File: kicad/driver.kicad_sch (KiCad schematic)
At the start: 72 parts, among them Q1 IRFZ44N, Q2 IRFZ44N, Q3 IRFZ44N, Q4 IRFZ44N, Q5 IRFZ44N, Q6 IRFZ44N, U1 IR2104, U2 IR2104, U3 IR2104, U4 INA180A2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

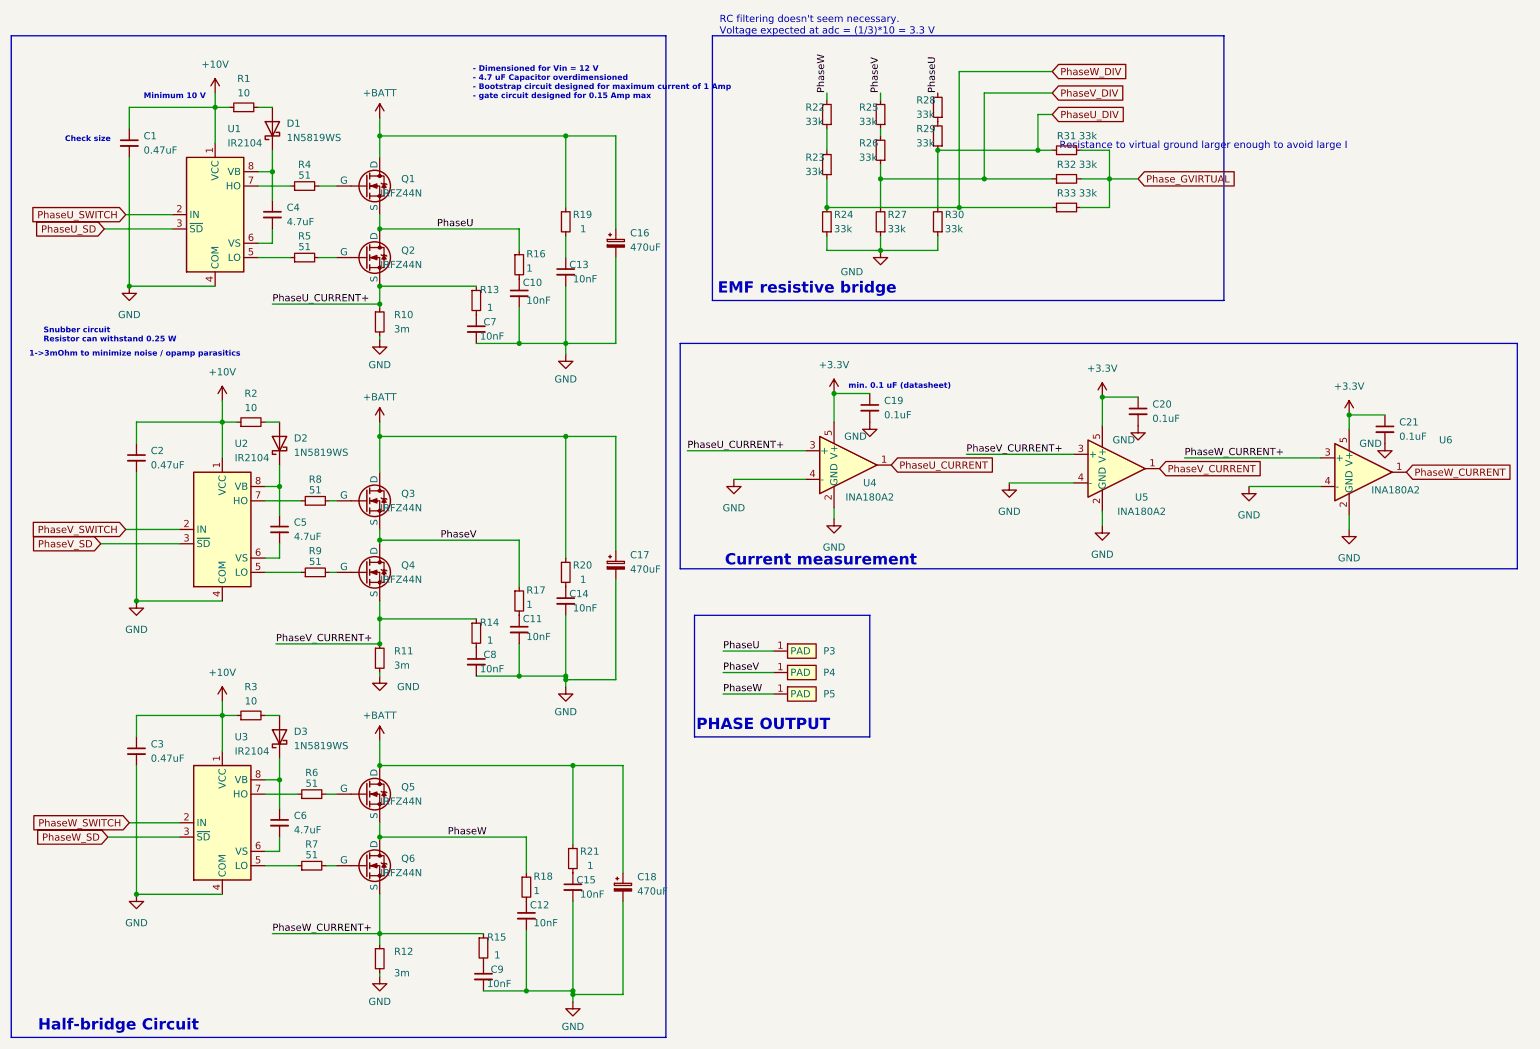
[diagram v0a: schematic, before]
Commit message: [bldc] Fixed footprint issues, added jlcpcb man. rules, stackup decisions, added nets..
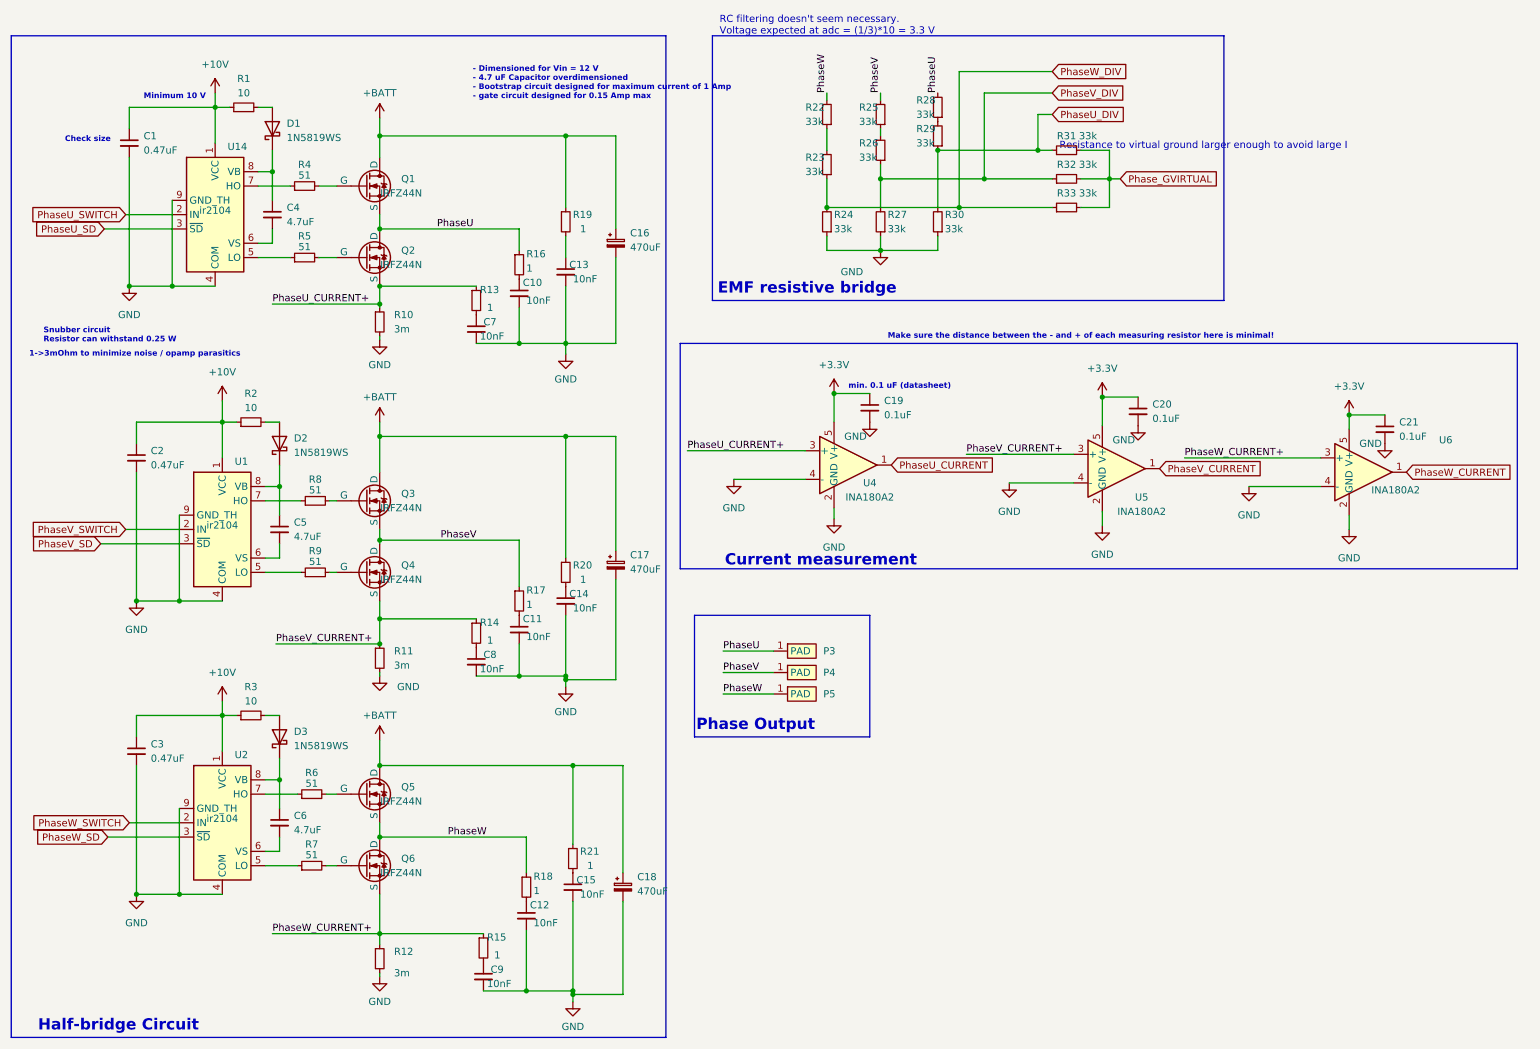
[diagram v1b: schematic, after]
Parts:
- removed U1, U2, U3: IR2104, Package_SO:SOIC-8-1EP_3.9x4.9mm_P1.27mm_EP2.29x3mm, symbol Driver_FET:IR2104
- added U1, U14, U2: ir2104, Package_SO:SOIC-8-1EP_3.9x4.9mm_P1.27mm_EP2.29x3mm, symbol bldc:ir2104_th
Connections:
- net +10V: now also U1.1 (VCC), U14.1 (VCC), U2.1 (VCC)
- net GND: now also U1.4 (COM), U1.9 (GND_TH), U14.4 (COM), U14.9 (GND_TH), U2.4 (COM), U2.9 (GND_TH)
- net PhaseU_SD: now also U14.3 (~{SD})
- net PhaseU_SWITCH: now also U14.2 (IN)
- net PhaseV_SD: now also U1.3 (~{SD})
- net PhaseV_SWITCH: now also U1.2 (IN)
- net PhaseW_SD: now also U2.3 (~{SD})
- net PhaseW_SWITCH: now also U2.2 (IN)
- net at R7.1: now also U2.5 (LO)
- net at C5.1, D2.1 (K): now also U1.8 (VB)
- net at C5.2: now also U1.6 (VS)
- net at R5.1: now also U14.5 (LO)
- net at C4.2: now also U14.6 (VS)
- net at R4.1: now also U14.7 (HO)
- net at C4.1, D1.1 (K): now also U14.8 (VB)
- net at R9.1: now also U1.5 (LO)
- net at C6.1, D3.1 (K): now also U2.8 (VB)
- net at R6.1: now also U2.7 (HO)
- net at C6.2: now also U2.6 (VS)
- net at R8.1: now also U1.7 (HO)
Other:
- note added: "Make sure the distance between the - and + of each measuring resistor here is minimal!"

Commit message: [kicad] basic placement of everything but power and inverter, changed the ldo, changed caps
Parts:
- renumbered P3 to P1, P4 to P2, P5 to P3, U14 to U1, U1 to U2, U2 to U3

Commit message: [kicad] Added silkscreen indicators for capacitors + screw terminal indications
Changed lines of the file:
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@@
   )
   (symbol (lib_name "ir2104_th_2") (lib_id "bldc:ir2104_th") (at 54.61 105.41 0) (unit 1)
-    (in_bom yes) (on_board yes) (dnp no) (fields_autoplaced)
+    (in_bom yes) (on_board yes) (dnp no)
     (property "Reference" "U2" (at 56.8041 93.345 0)
       (effects (font (size 1.27 1.27)) (justify left))
@@
       (effects (font (size 1.27 1.27)) (justify bottom))
     )
-    (property "Footprint" "Package_SO:SOIC-8-1EP_3.9x4.9mm_P1.27mm_EP2.29x3mm" (at 54.61 105.41 0)
+    (property "Footprint" "Package_SO:SOIC-8-1EP_3.9x4.9mm_P1.27mm_EP2.29x3mm" (at 49.53 125.73 0)
       (effects (font (size 1.27 1.27)) (justify bottom) hide)
     )
@@
     )
     (property "Footprint" "Package_SO:SOIC-8-1EP_3.9x4.9mm_P1.27mm_EP2.29x3mm" (at 53.34 49.53 0)
-      (effects (font (size 1.27 1.27)) (justify bottom) hide)
+      (effects (font (size 1.27 1.27)) (justify bottom))
     )
     (property "Datasheet" "file:///home/igorwolfs/Downloads/1.translated.pdf" (at 53.34 49.53 0)

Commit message: [kicad] TODO: add silkscreen to FET-drivers, tantalum capacitors (check this first), FETs and other polar components OR check with manufacturer
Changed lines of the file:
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@@
     )
     (property "Footprint" "Package_SO:SOIC-8-1EP_3.9x4.9mm_P1.27mm_EP2.29x3mm" (at 53.34 49.53 0)
-      (effects (font (size 1.27 1.27)) (justify bottom))
+      (effects (font (size 1.27 1.27)) (justify bottom) hide)
     )
     (property "Datasheet" "file:///home/igorwolfs/Downloads/1.translated.pdf" (at 53.34 49.53 0)

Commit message: [kicad] Done first set of footprint checks, adapted connector to regular phoenix connector, found 3d models for everything but button [scripts] Checked resonator calculation [simulations] Checked bootstrap simulation [cubemx] Added extra GPIO-input + checked cpu pins
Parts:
- U4, U5, U6: value INA180A2 -> INA180A2IDBVR; MFR.Part (none) -> INA180A2IDBVR
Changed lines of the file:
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@@
       (effects (font (size 1.27 1.27)))
     )
-    (property "Value" "INA180A2" (at 262.89 98.425 0)
+    (property "Value" "INA180A2IDBVR" (at 262.89 98.425 0)
       (effects (font (size 1.27 1.27)))
     )
@@
       (effects (font (size 1.27 1.27)) hide)
     )
-    (property "JLCPCB" "" (at 257.175 95.25 0)
-      (effects (font (size 1.27 1.27)) hide)
-    )
     (property "jlcpcb" "C192764" (at 257.175 95.25 0)
+      (effects (font (size 1.27 1.27)) hide)
+    )
+    (property "MFR.Part" "INA180A2IDBVR" (at 257.175 95.25 0)
       (effects (font (size 1.27 1.27)) hide)
     )
@@
       (effects (font (size 1.27 1.27)))
     )
-    (property "Value" "INA180A2" (at 169.545 99.695 0)
+    (property "Value" "INA180A2IDBVR" (at 169.545 99.695 0)
       (effects (font (size 1.27 1.27)))
     )
@@
       (effects (font (size 1.27 1.27)) hide)
     )
-    (property "JLCPCB" "" (at 165.735 93.98 0)
-      (effects (font (size 1.27 1.27)) hide)
-    )
     (property "jlcpcb" "C192764" (at 165.735 93.98 0)
+      (effects (font (size 1.27 1.27)) hide)
+    )
+    (property "MFR.Part" "INA180A2IDBVR" (at 165.735 93.98 0)
       (effects (font (size 1.27 1.27)) hide)
     )
@@
       (effects (font (size 1.27 1.27)))
     )
-    (property "Value" "INA180A2" (at 217.805 102.235 0)
+    (property "Value" "INA180A2IDBVR" (at 217.805 102.235 0)
       (effects (font (size 1.27 1.27)))
     )
@@
       (effects (font (size 1.27 1.27)) hide)
     )
-    (property "JLCPCB" "" (at 213.36 94.615 0)
-      (effects (font (size 1.27 1.27)) hide)
-    )
     (property "jlcpcb" "C192764" (at 213.36 94.615 0)
       (effects (font (size 1.27 1.27)) hide)
     )
+    (property "MFR.Part" "INA180A2IDBVR" (at 213.36 94.615 0)
+      (effects (font (size 1.27 1.27)) hide)
+    )

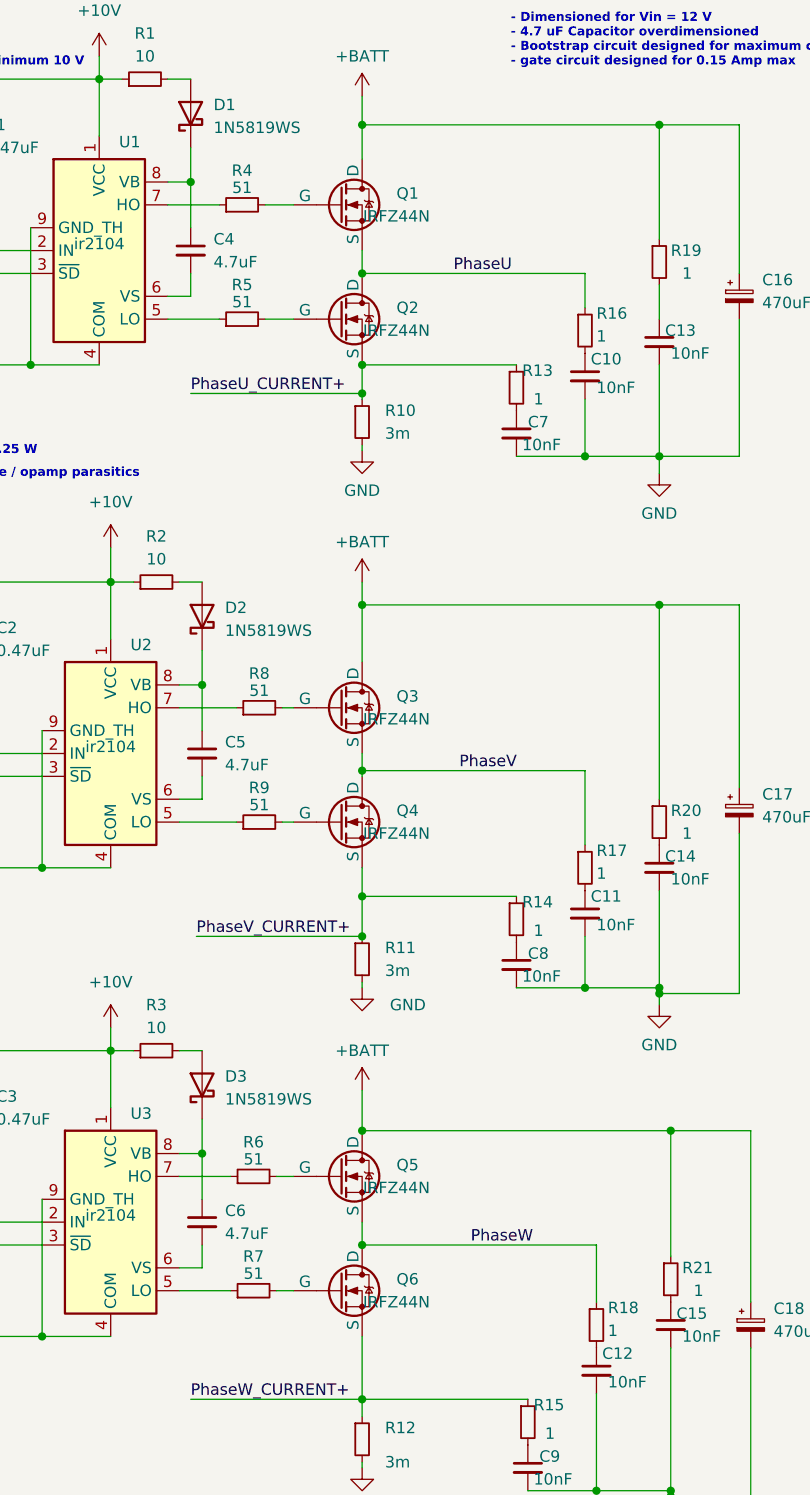
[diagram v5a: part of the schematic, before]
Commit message: changed inductors, rearranged new FET footprints and symbols
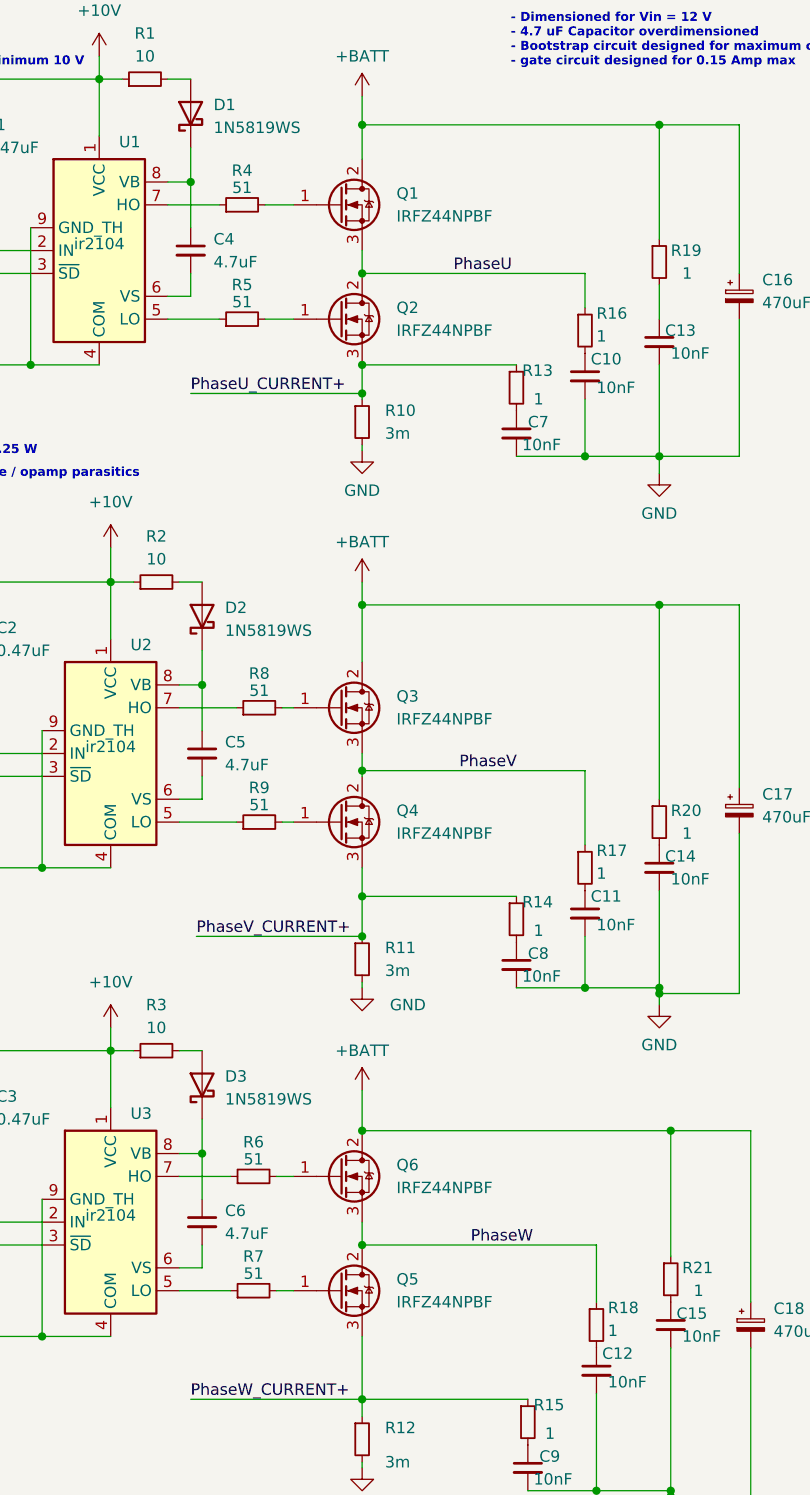
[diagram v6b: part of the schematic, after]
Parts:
- removed Q1, Q2, Q3, Q4, Q5, Q6: IRFZ44N, Package_TO_SOT_THT:TO-220-3_Vertical, symbol Simulation_SPICE:NMOS
- added Q1, Q2, Q3, Q4, Q5, Q6: IRFZ44NPBF, Package_TO_SOT_THT:TO-220-3_Vertical, symbol bldc:IRFZ44N
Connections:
- net +BATT: now also Q1.2 (D), Q3.2 (D), Q6.2 (D)
- net PhaseU: now also Q1.3 (S), Q2.2 (D)
- net PhaseU_CURRENT+: now also Q2.3 (S)
- net PhaseV: now also Q3.3 (S), Q4.2 (D)
- net PhaseV_CURRENT+: now also Q4.3 (S)
- net PhaseW: now also Q5.2 (D), Q6.3 (S)
- net PhaseW_CURRENT+: now also Q5.3 (S)
- net at R7.2: now also Q5.1 (G)
- net at R9.2: now also Q4.1 (G)
- net at R6.2: now also Q6.1 (G)
- net at R4.2: now also Q1.1 (G)
- net at R8.2: now also Q3.1 (G)
- net at R5.2: now also Q2.1 (G)
